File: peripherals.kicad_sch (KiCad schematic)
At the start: 47 parts, among them J15 Molex_PicoBlade_1x4_0533980471, J16 JST_SH_1x4_SM04B-SRSS-TB-LF-SN, J17 JST_SH_1x4_SM04B-SRSS-TB-LF-SN, Q13 PJE138K, Q14 PJE138K, U14 SLB9673AU20FW2610XTMA1, U51 NTS0102_XSON, U53 AP22653_DFN, U54 M24C64-F_DFN8, U55 AP22653_DFN

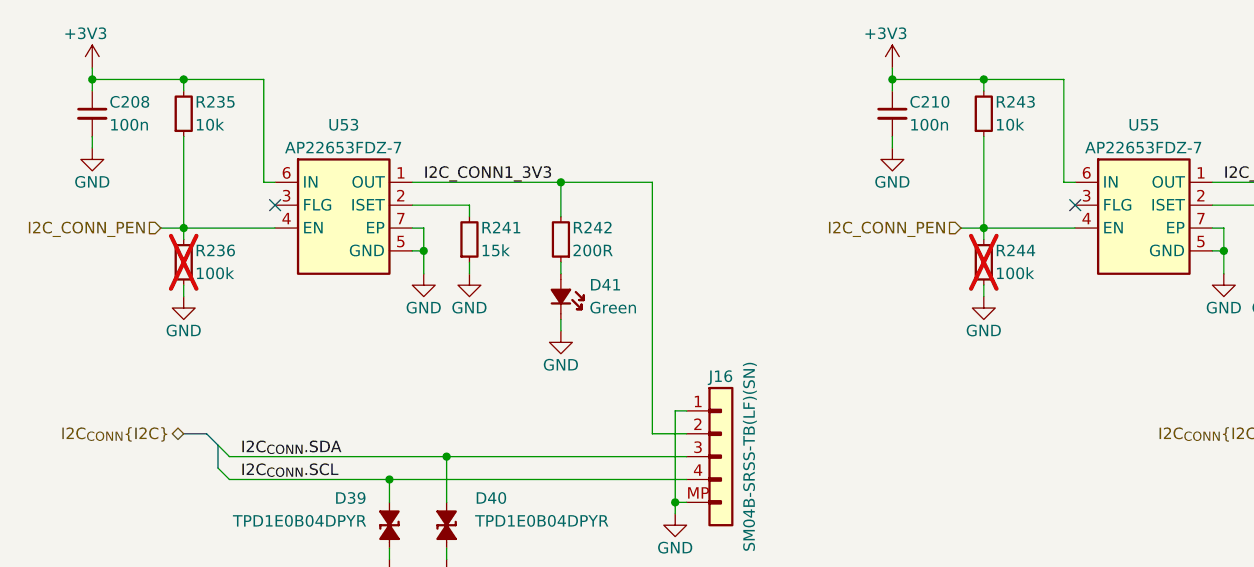
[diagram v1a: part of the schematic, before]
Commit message: [#83396] Implement small post review fixes eg. correct LED resistor values, update sheet table, delete four wire connections
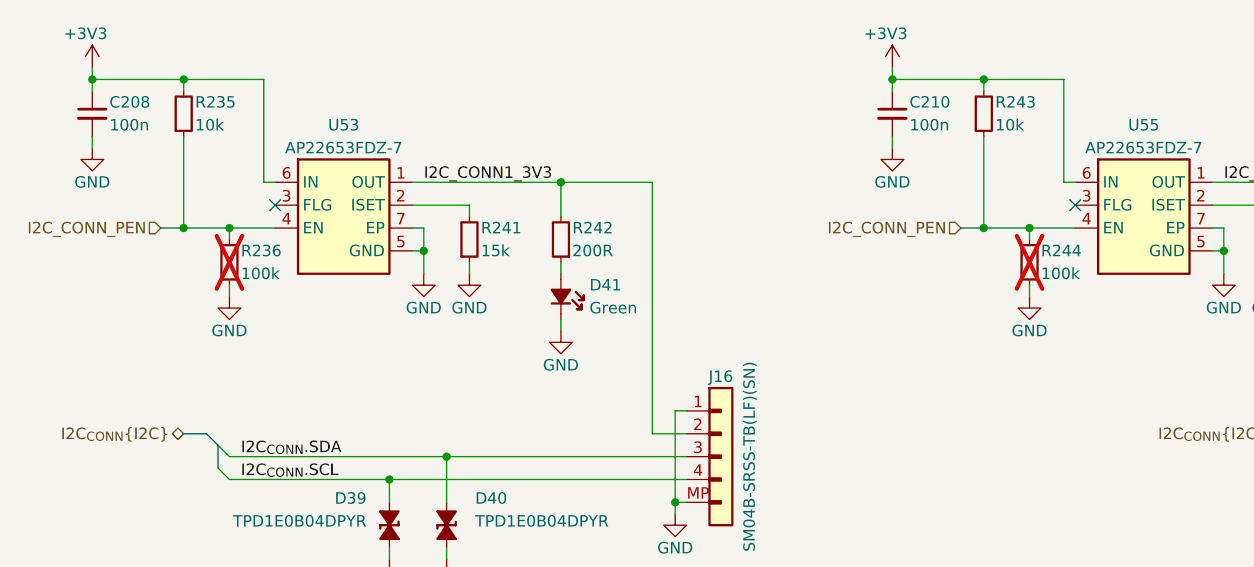
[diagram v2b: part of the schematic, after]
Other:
- moved on the sheet: R236, R244
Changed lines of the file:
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@@
 	)
 	(junction
+		(at 279.4 54.61)
+		(diameter 0)
+		(color 0 0 0 0)
+	)
+	(junction
+		(at 190.5 54.61)
+		(diameter 0)
+		(color 0 0 0 0)
+	)
+	(junction
 		(at 240.03 85.09)
 		(diameter 0)
@@
 	(wire
 		(pts
+			(xy 279.4 54.61) (xy 284.48 54.61)
+		)
+		(stroke
+			(width 0)
+			(type default)
+		)
+	)
+	(wire
+		(pts
 			(xy 27.94 220.98) (xy 44.45 220.98)
 		)
@@
 	(wire
 		(pts
-			(xy 185.42 60.96) (xy 185.42 62.23)
+			(xy 190.5 60.96) (xy 190.5 62.23)
 		)
 		(stroke
@@
 	(wire
 		(pts
-			(xy 274.32 54.61) (xy 284.48 54.61)
+			(xy 274.32 54.61) (xy 279.4 54.61)
 		)
 		(stroke
@@
 	(wire
 		(pts
-			(xy 185.42 54.61) (xy 195.58 54.61)
+			(xy 185.42 54.61) (xy 190.5 54.61)
 		)
 		(stroke
@@
 	(wire
 		(pts
-			(xy 274.32 54.61) (xy 274.32 55.88)
+			(xy 279.4 54.61) (xy 279.4 55.88)
 		)
 		(stroke
@@
 	(wire
 		(pts
-			(xy 185.42 54.61) (xy 185.42 55.88)
+			(xy 190.5 54.61) (xy 190.5 55.88)
 		)
 		(stroke
@@
 	(wire
 		(pts
+			(xy 190.5 54.61) (xy 195.58 54.61)
+		)
+		(stroke
+			(width 0)
+			(type default)
+		)
+	)
+	(wire
+		(pts
 			(xy 195.58 151.13) (xy 195.58 153.67)
 		)
@@
 	(wire
 		(pts
-			(xy 274.32 60.96) (xy 274.32 62.23)
+			(xy 279.4 60.96) (xy 279.4 62.23)
 		)
 		(stroke
@@
 	(symbol
 		(lib_id "antmicroResistors0402:R_100k_0402")
-		(at 185.42 60.96 90)
+		(at 190.5 60.96 90)
 		(unit 1)
 		(exclude_from_sim no)
@@
 		(dnp yes)
 		(property "Reference" "R236"
-			(at 186.69 57.15 90)
+			(at 191.77 57.15 90)
 			(effects
 				(font
@@
 		)
 		(property "Value" "R_100k_0402"
-			(at 198.12 40.64 0)
+			(at 203.2 40.64 0)
 			(effects
 				(font
@@
 		)
 		(property "Footprint" "antmicro-footprints:R_0402_1005Metric"
-			(at 200.66 40.64 0)
+			(at 205.74 40.64 0)
 			(effects
 				(font
@@
 		)
 		(property "Datasheet" "https://www.bourns.com/docs/product-datasheets/cr.pdf"
-			(at 203.2 40.64 0)
+			(at 208.28 40.64 0)
 			(effects
 				(font
@@
 		)
 		(property "Description" "SMD Chip Resistor, 100 kohm, ± 1%, 62.5 mW, 0402 [1005 Metric], Thick Film, General Purpose"
-			(at 185.42 60.96 0)
+			(at 190.5 60.96 0)
 			(effects
 				(font
@@
 		)
 		(property "Manufacturer" "Bourns"
-			(at 208.28 40.64 0)
+			(at 213.36 40.64 0)
 			(effects
 				(font
@@
 		)
 		(property "MPN" "CR0402-FX-1003GLF"
-			(at 205.74 40.64 0)
+			(at 210.82 40.64 0)
 			(effects
 				(font
@@
 		)
 		(property "Val" "100k"
-			(at 186.69 59.69 90)
+			(at 191.77 59.69 90)
 			(effects
 				(font
@@
 		)
 		(property "License" "Apache-2.0"
-			(at 210.82 40.64 0)
+			(at 215.9 40.64 0)
 			(effects
 				(font
@@
 		)
 		(property "Author" "Antmicro"
-			(at 213.36 40.64 0)
+			(at 218.44 40.64 0)
 			(effects
 				(font
@@
 		)
 		(property "Tolerance" "1%"
-			(at 195.58 40.64 0)
+			(at 200.66 40.64 0)
 			(effects
 				(font
@@
 	(symbol
 		(lib_id "antmicropower:GND")
-		(at 274.32 62.23 0)
+		(at 279.4 62.23 0)
 		(unit 1)
 		(exclude_from_sim no)
@@
 		(fields_autoplaced yes)
 		(property "Reference" "#PWR0420"
-			(at 274.32 68.58 0)
+			(at 279.4 68.58 0)
 			(effects
 				(font
@@
 		)
 		(property "Value" "GND"
-			(at 274.32 66.04 0)
+			(at 279.4 66.04 0)
 			(effects
 				(font
@@
 		)
 		(property "Footprint" ""
-			(at 283.21 69.85 0)
+			(at 288.29 69.85 0)
 			(effects
 				(font
@@
 		)
 		(property "Datasheet" ""
-			(at 283.21 74.93 0)
+			(at 288.29 74.93 0)
 			(effects
 				(font
@@
 		)
 		(property "Description" ""
-			(at 274.32 62.23 0)
+			(at 279.4 62.23 0)
 			(effects
 				(font
@@
 		)
 		(property "Author" "Antmicro"
-			(at 283.21 69.85 0)
+			(at 288.29 69.85 0)
 			(effects
 				(font
@@
 		)
 		(property "License" "Apache-2.0"
-			(at 283.21 72.39 0)
+			(at 288.29 72.39 0)
 			(effects
 				(font
@@
 	(symbol
 		(lib_id "antmicropower:GND")
-		(at 185.42 62.23 0)
+		(at 190.5 62.23 0)
 		(unit 1)
 		(exclude_from_sim no)
@@
 		(fields_autoplaced yes)
 		(property "Reference" "#PWR0403"
-			(at 185.42 68.58 0)
+			(at 190.5 68.58 0)
 			(effects
 				(font
@@
 		)
 		(property "Value" "GND"
-			(at 185.42 66.04 0)
+			(at 190.5 66.04 0)
 			(effects
 				(font
@@
 		)
 		(property "Footprint" ""
-			(at 194.31 69.85 0)
+			(at 199.39 69.85 0)
 			(effects
 				(font
@@
 		)
 		(property "Datasheet" ""
-			(at 194.31 74.93 0)
+			(at 199.39 74.93 0)
 			(effects
 				(font
@@
 		)
 		(property "Description" ""
-			(at 185.42 62.23 0)
+			(at 190.5 62.23 0)
 			(effects
 				(font
@@
 		)
 		(property "Author" "Antmicro"
-			(at 194.31 69.85 0)
+			(at 199.39 69.85 0)
 			(effects
 				(font
@@
 		)
 		(property "License" "Apache-2.0"
-			(at 194.31 72.39 0)
+			(at 199.39 72.39 0)
 			(effects
 				(font
@@
 	(symbol
 		(lib_id "antmicroResistors0402:R_100k_0402")
-		(at 274.32 60.96 90)
+		(at 279.4 60.96 90)
 		(unit 1)
 		(exclude_from_sim no)
@@
 		(dnp yes)
 		(property "Reference" "R244"
-			(at 275.59 57.15 90)
+			(at 280.67 57.15 90)
 			(effects
 				(font
@@
 		)
 		(property "Value" "R_100k_0402"
-			(at 287.02 40.64 0)
+			(at 292.1 40.64 0)
 			(effects
 				(font
@@
 		)
 		(property "Footprint" "antmicro-footprints:R_0402_1005Metric"
-			(at 289.56 40.64 0)
+			(at 294.64 40.64 0)
 			(effects
 				(font
@@
 		)
 		(property "Datasheet" "https://www.bourns.com/docs/product-datasheets/cr.pdf"
-			(at 292.1 40.64 0)
+			(at 297.18 40.64 0)
 			(effects
 				(font
@@
 		)
 		(property "Description" "SMD Chip Resistor, 100 kohm, ± 1%, 62.5 mW, 0402 [1005 Metric], Thick Film, General Purpose"
-			(at 274.32 60.96 0)
+			(at 279.4 60.96 0)
 			(effects
 				(font
@@
 		)
 		(property "Manufacturer" "Bourns"
-			(at 297.18 40.64 0)
+			(at 302.26 40.64 0)
 			(effects
 				(font
@@
 		)
 		(property "MPN" "CR0402-FX-1003GLF"
-			(at 294.64 40.64 0)
+			(at 299.72 40.64 0)
 			(effects
 				(font
@@
 		)
 		(property "Val" "100k"
-			(at 275.59 59.69 90)
+			(at 280.67 59.69 90)
 			(effects
 				(font
@@
 		)
 		(property "License" "Apache-2.0"
-			(at 299.72 40.64 0)
+			(at 304.8 40.64 0)
 			(effects
 				(font
@@
 		)
 		(property "Author" "Antmicro"
-			(at 302.26 40.64 0)
+			(at 307.34 40.64 0)
 			(effects
 				(font
@@
 		)
 		(property "Tolerance" "1%"
-			(at 284.48 40.64 0)
+			(at 289.56 40.64 0)
 			(effects
 				(font

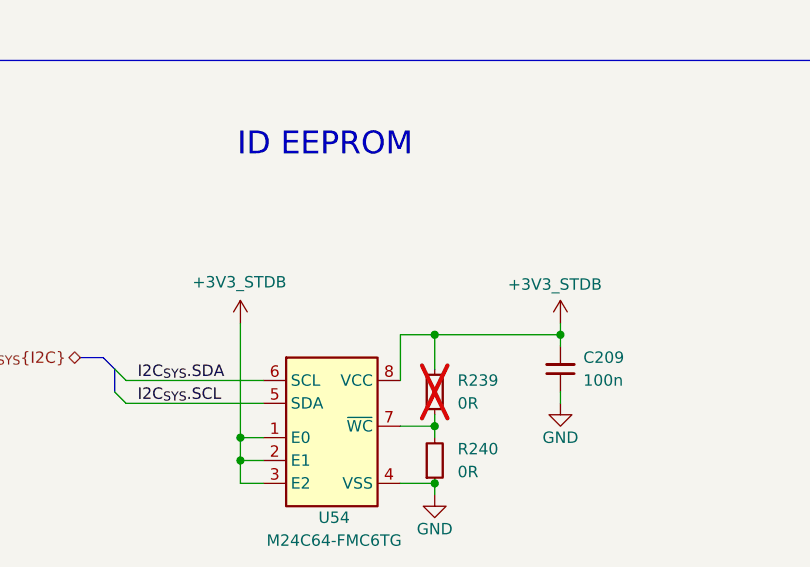
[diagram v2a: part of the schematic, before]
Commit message: [#83396] Continue post review fixes according power and M.2
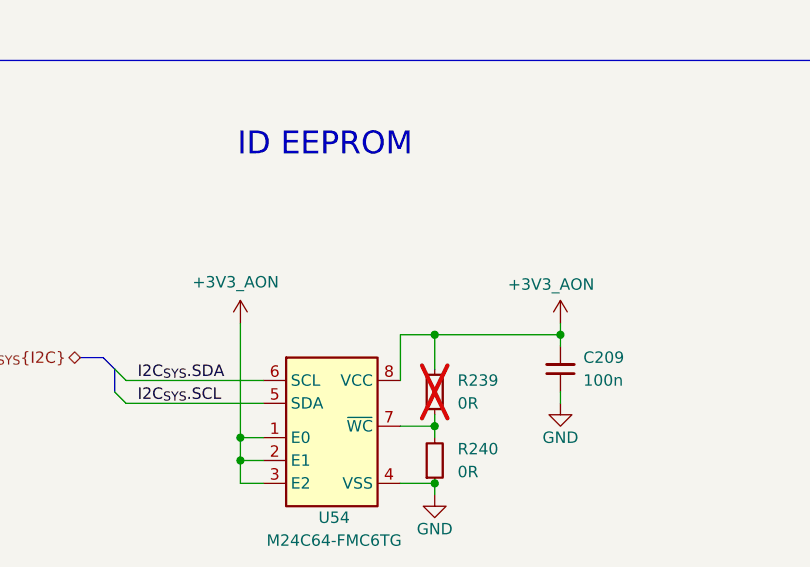
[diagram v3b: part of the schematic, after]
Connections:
- net +3V3_STDB renamed +3V3_AON
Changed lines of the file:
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@@
 			)
 		)
-		(property "Value" "+3V3_STDB"
+		(property "Value" "+3V3_AON"
 			(at 190.246 131.318 0)
 			(effects
@@
 			)
 		)
-		(property "Value" "+3V3_STDB"
+		(property "Value" "+3V3_AON"
 			(at 225.298 131.572 0)
 			(effects

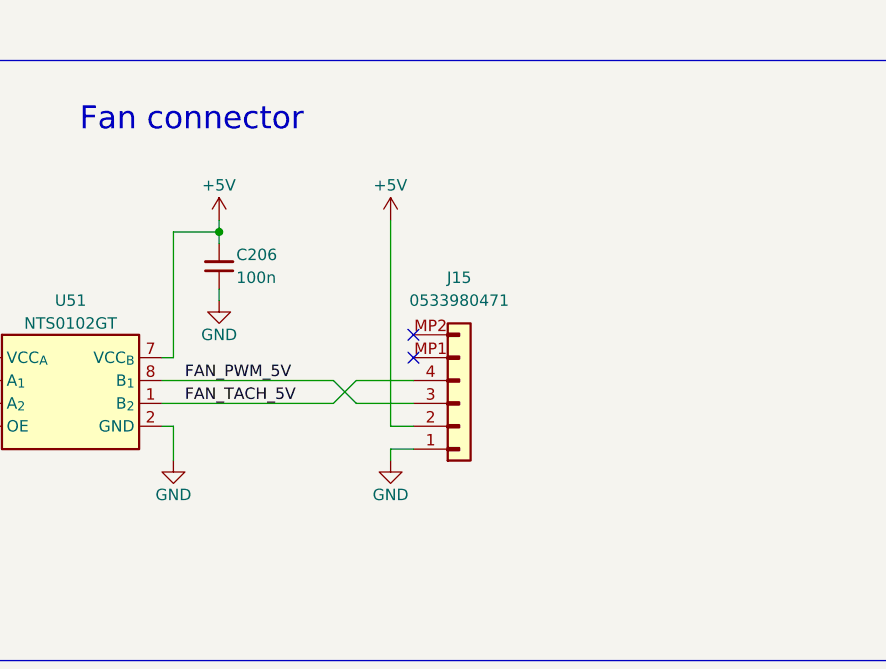
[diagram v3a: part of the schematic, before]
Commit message: [#84355] Add 12V to fan and expansion connector
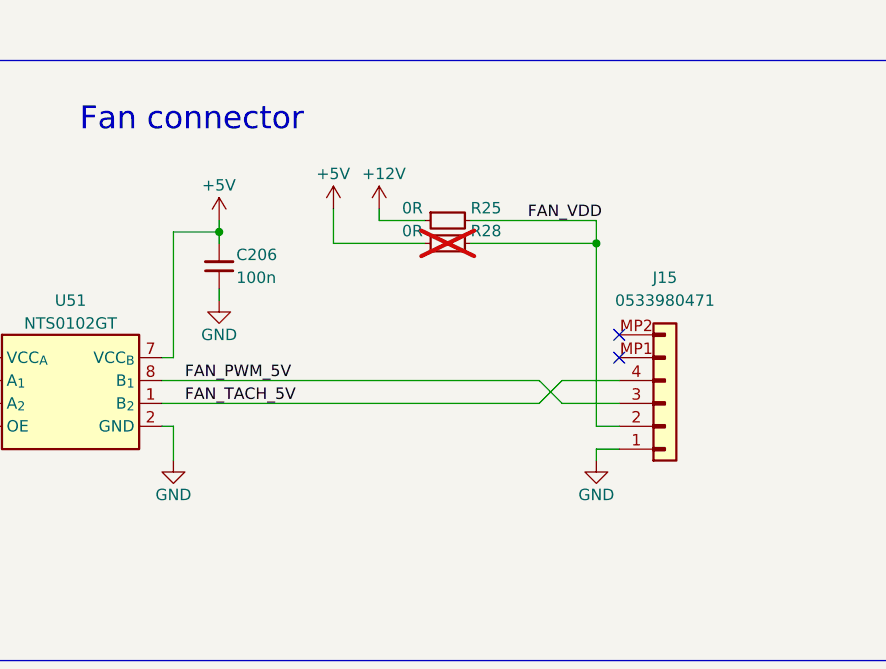
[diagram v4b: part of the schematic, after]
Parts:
- added R25, R28: R_0R_0402, antmicro-footprints:R_0402_1005Metric, symbol antmicroResistors0402:R_0R_0402
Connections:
- net +5V: now also R28.1; no longer J15.2
- new net +12V: R25.1
- new net FAN_VDD: J15.2, R25.2, R28.2
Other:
- moved on the sheet: J15

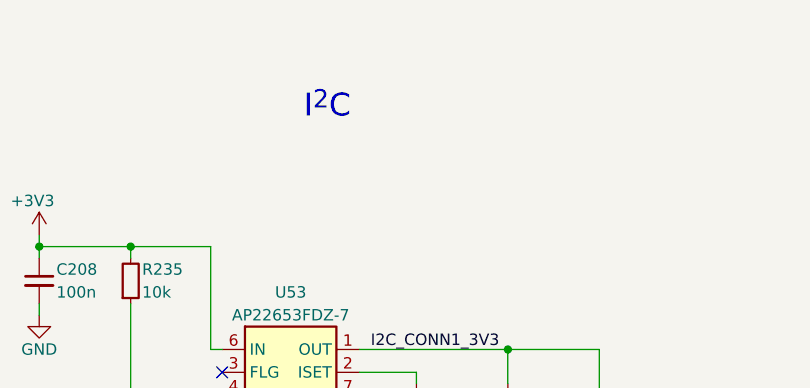
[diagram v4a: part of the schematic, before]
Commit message: [#84355] Clear ERC problems
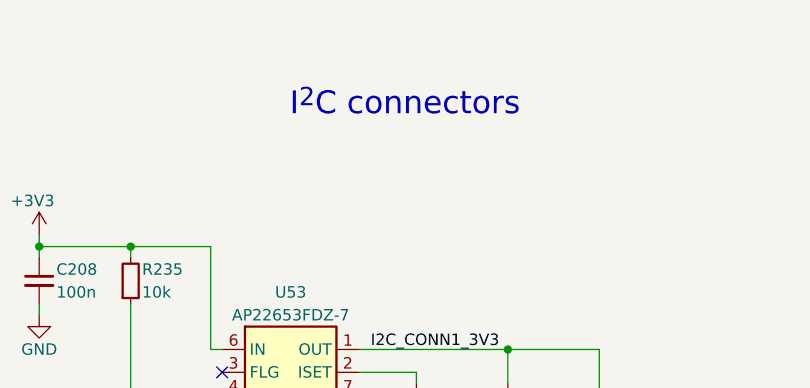
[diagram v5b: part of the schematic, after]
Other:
- note added: "I^{2}C connectors"
- note removed: "I^{2}C"
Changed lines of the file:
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@@
 		)
 	)
-	(text "I^{2}C"
+	(text "I^{2}C connectors"
 		(exclude_from_sim no)
-		(at 207.264 22.606 0)
+		(at 215.9 22.352 0)
 		(effects
 			(font

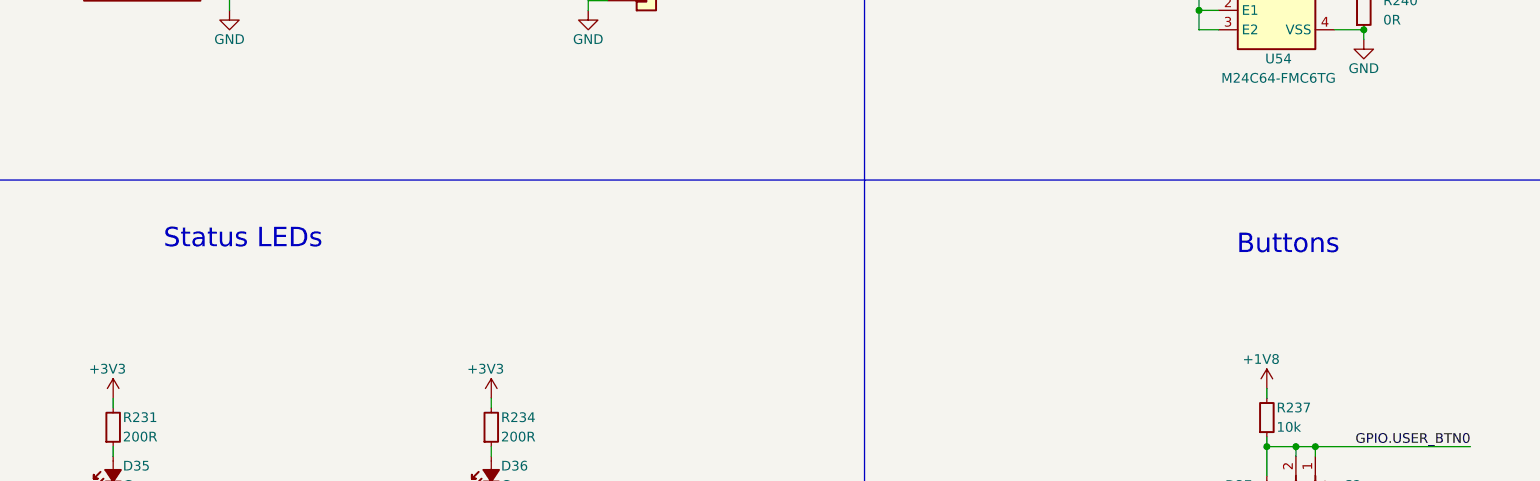
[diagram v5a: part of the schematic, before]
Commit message: [#82846] Align designators
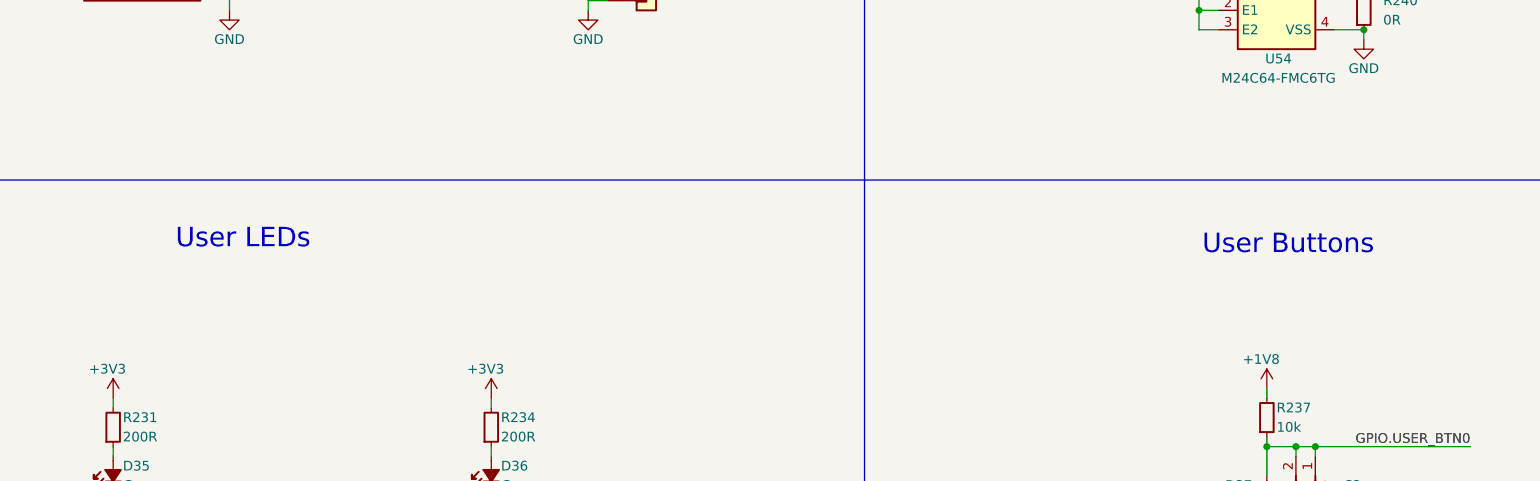
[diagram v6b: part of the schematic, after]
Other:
- note added: "User Buttons"
- note added: "User LEDs"
- note removed: "Buttons"
- note removed: "Status LEDs"
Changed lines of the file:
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@@
 	(title_block
 		(title "Jetson AGX Thor Baseboard")
-		(date "2025-08-11")
+		(date "2025-10-08")
 		(rev "1.0.0")
 		(company "Antmicro Ltd")
@@
 		)
 	)
-	(text "Buttons"
+	(text "User Buttons"
 		(exclude_from_sim no)
 		(at 207.264 181.864 0)
@@
 		)
 	)
-	(text "Status LEDs"
+	(text "User LEDs"
 		(exclude_from_sim no)
 		(at 70.358 181.102 0)
